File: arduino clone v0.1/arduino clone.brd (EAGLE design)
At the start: 72.9 x 27.6 mm, 47 parts, among them J203 ICSP HEADER, J402 FTDI Breakout Header, U101 ATMEGA328P_TQFP, U301 CH340G, Y101 16MHz, Y301 12MHz

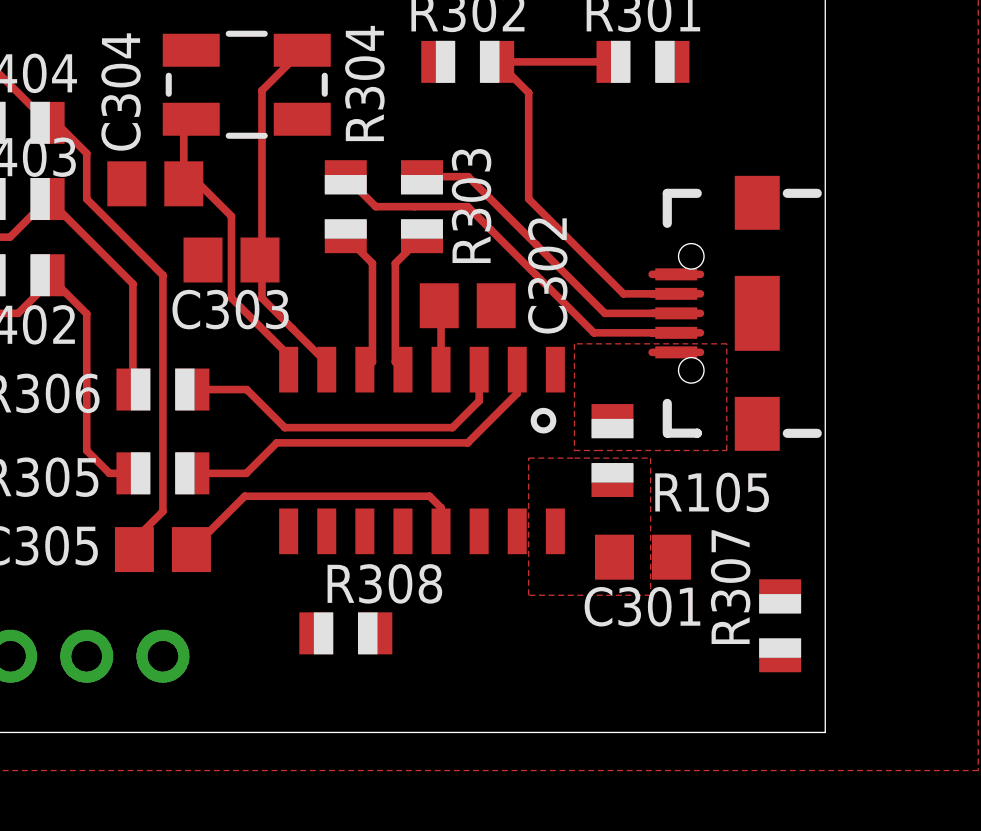
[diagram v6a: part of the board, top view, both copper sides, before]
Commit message: route and place R308 and R307
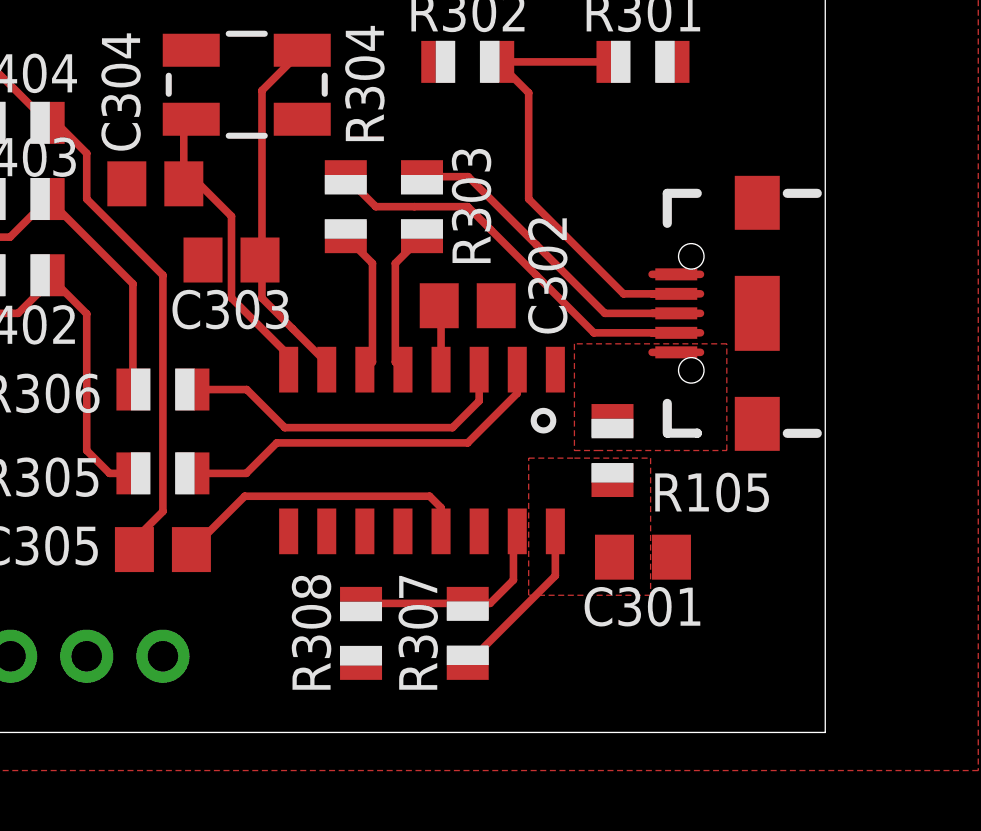
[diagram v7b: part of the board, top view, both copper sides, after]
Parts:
- moved R307 10.4 mm to (69.8, 41.4), turned to 270 degrees
- moved R308 0.51 mm to (66.3, 41.4), turned to 90 degrees
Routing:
- net CH340G_R232: track 0.00 -> 7.08 mm
- net PP5V0_CH340G: track 0.00 -> 5.61 mm
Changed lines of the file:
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@@
 <attribute name="NAME" x="53.594" y="48.768" size="1.27" layer="25"/>
 </element>
-<element name="R307" library="adafruit" package="R0805" value="10k" x="80.264" y="41.656" smashed="yes" rot="R90">
-<attribute name="NAME" x="79.248" y="40.894" size="1.27" layer="25" rot="R90"/>
-<attribute name="STUFF" value="NO STUFF" x="80.264" y="41.656" size="1.778" layer="27" rot="R90" display="off"/>
-</element>
-<element name="R308" library="adafruit" package="R0805" value="10k" x="65.786" y="41.402" smashed="yes">
-<attribute name="NAME" x="65.024" y="42.418" size="1.27" layer="25"/>
-<attribute name="STUFF" value="NO STUFF" x="65.786" y="41.402" size="1.778" layer="27" display="off"/>
+<element name="R307" library="adafruit" package="R0805" value="10k" x="69.85" y="41.402" smashed="yes" rot="R270">
+<attribute name="NAME" x="68.834" y="39.37" size="1.27" layer="25" rot="R90"/>
+<attribute name="STUFF" value="NO STUFF" x="69.85" y="41.402" size="1.778" layer="27" rot="R270" display="off"/>
+</element>
+<element name="R308" library="adafruit" package="R0805" value="10k" x="66.294" y="41.402" smashed="yes" rot="R90">
+<attribute name="NAME" x="65.278" y="39.37" size="1.27" layer="25" rot="R90"/>
+<attribute name="STUFF" value="NO STUFF" x="66.294" y="41.402" size="1.778" layer="27" rot="R90" display="off"/>
 </element>
 <element name="R401" library="adafruit" package="R0805" value="0" x="45.974" y="49.276" smashed="yes" rot="R270">
@@
 <vertex x="71.882" y="47.244"/>
 </polygon>
-<wire x1="74.742" y1="43.942" x2="80.264" y2="42.656" width="0" layer="19" extent="1-1"/>
+<wire x1="69.85" y1="40.402" x2="72.771" y2="43.323" width="0.254" layer="1"/>
+<wire x1="72.771" y1="43.323" x2="72.771" y2="44.803" width="0.254" layer="1"/>
 </signal>
 <signal name="PP3V3_CH340G">
@@
 <contactref element="R307" pad="1"/>
 <contactref element="R308" pad="2"/>
-<wire x1="71.501" y1="44.803" x2="80.264" y2="40.656" width="0" layer="19" extent="1-1"/>
-<wire x1="66.786" y1="41.402" x2="71.501" y2="44.803" width="0" layer="19" extent="1-1"/>
+<wire x1="66.294" y1="42.402" x2="69.85" y2="42.402" width="0.254" layer="1"/>
+<wire x1="71.501" y1="44.803" x2="71.374" y2="44.676" width="0.254" layer="1"/>
+<wire x1="71.374" y1="44.676" x2="71.374" y2="43.18" width="0.254" layer="1"/>
+<wire x1="71.374" y1="43.18" x2="70.596" y2="42.402" width="0.254" layer="1"/>
+<wire x1="70.596" y1="42.402" x2="69.85" y2="42.402" width="0.254" layer="1"/>
 </signal>
 <signal name="CH340G_XTAL_IN">
@@
 <wire x1="60.634" y1="58.54" x2="60.386" y2="58.292" width="0.254" layer="1"/>
 <wire x1="60.386" y1="58.292" x2="60.386" y2="56.388" width="0.254" layer="1"/>
-<wire x1="60.386" y1="56.388" x2="60.706" y2="56.388" width="0.254" layer="1"/>
 <wire x1="61.976" y1="55.306" x2="60.894" y2="56.388" width="0.254" layer="1"/>
 <wire x1="63.881" y1="50.193" x2="63.881" y2="50.673" width="0.254" layer="1"/>

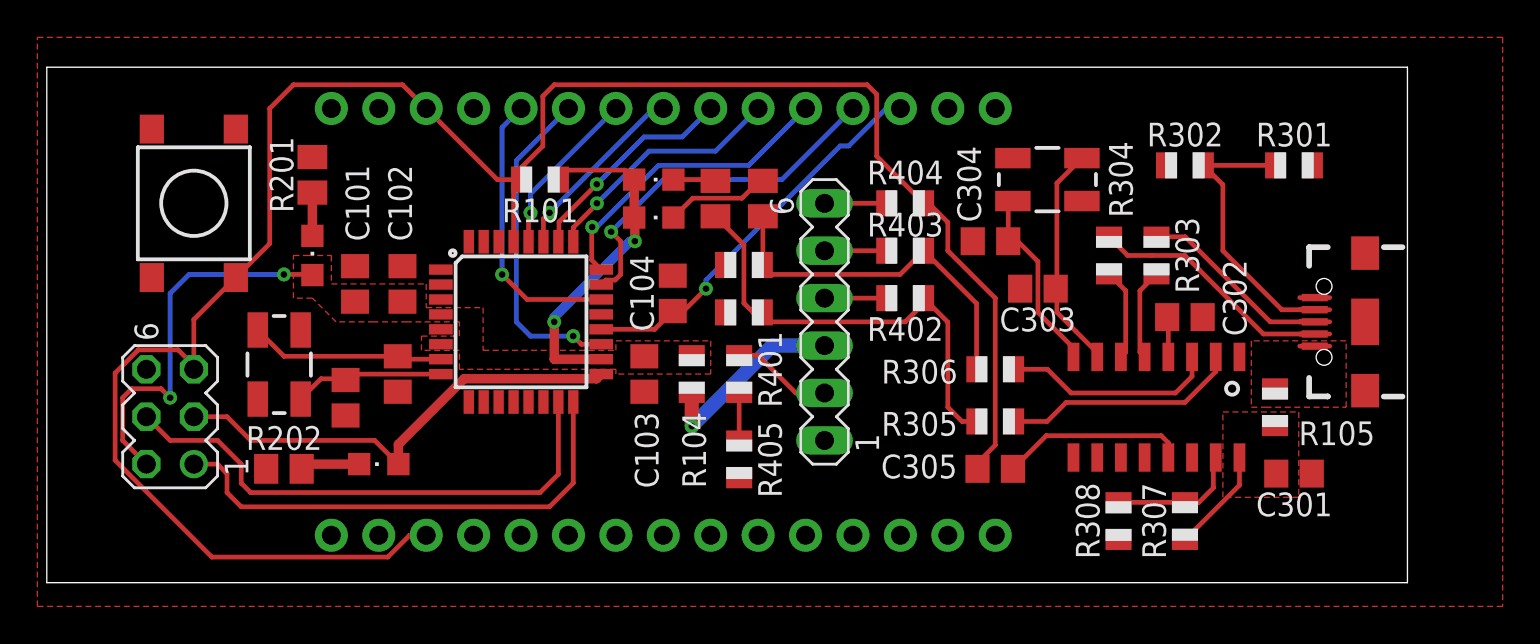
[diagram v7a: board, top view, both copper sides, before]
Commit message: add PP5V0_USB trace from USB port to FTDI header
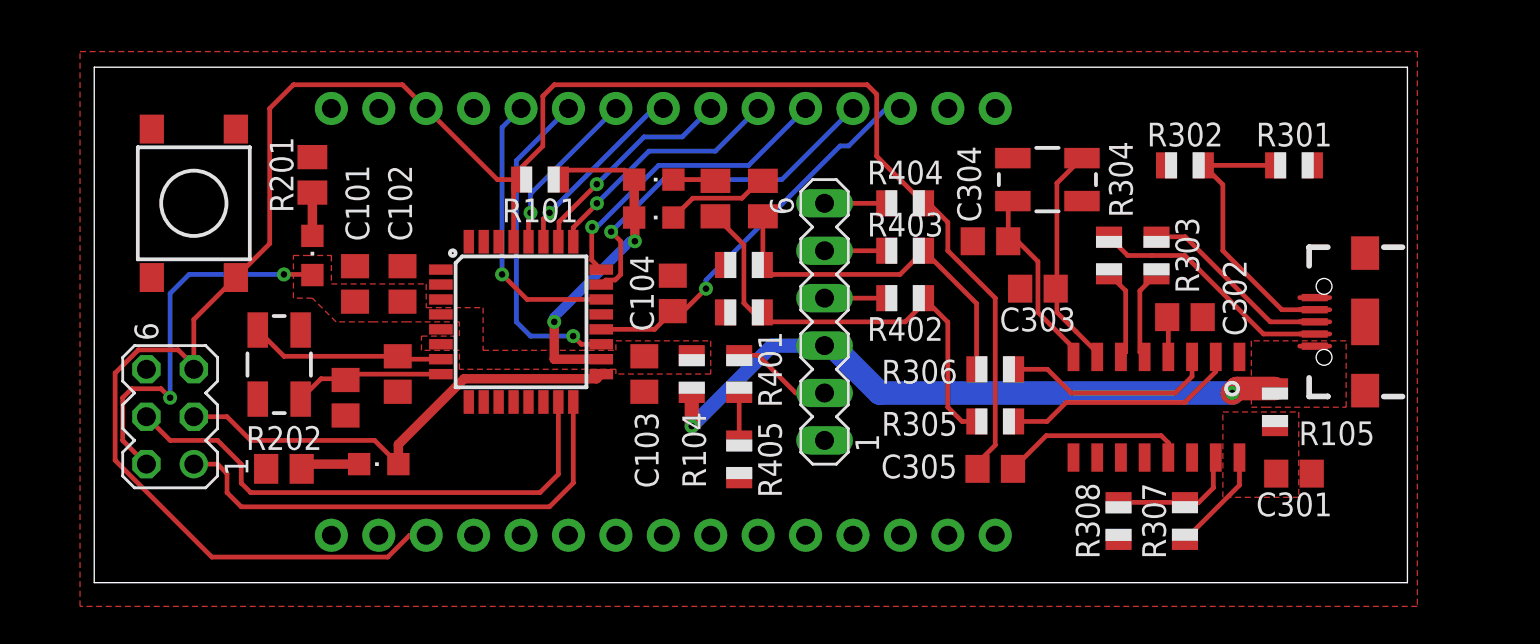
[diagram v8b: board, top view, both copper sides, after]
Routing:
- net PP5V0_USB: track 10.7 -> 36.0 mm, vias 1 -> 2
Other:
- board size 72.9 x 27.6 mm -> 70.3 x 27.6 mm
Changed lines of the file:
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@@
 <board>
 <plain>
-<wire x1="8.89" y1="38.1" x2="81.768" y2="38.1" width="0" layer="20"/>
+<wire x1="11.43" y1="38.1" x2="81.768" y2="38.1" width="0" layer="20"/>
 <wire x1="81.768" y1="38.1" x2="81.768" y2="65.71" width="0" layer="20"/>
-<wire x1="81.768" y1="65.71" x2="8.89" y2="65.71" width="0" layer="20"/>
-<wire x1="8.89" y1="65.71" x2="8.89" y2="38.1" width="0" layer="20"/>
+<wire x1="81.768" y1="65.71" x2="11.43" y2="65.71" width="0" layer="20"/>
+<wire x1="11.43" y1="65.71" x2="11.43" y2="38.1" width="0" layer="20"/>
 </plain>
 <attributes>
@@
 <contactref element="R202" pad="1"/>
 <polygon width="0.0762" layer="1" rank="6">
-<vertex x="8.382" y="67.31"/>
-<vertex x="86.868" y="67.31"/>
-<vertex x="86.868" y="36.83"/>
-<vertex x="8.382" y="36.83"/>
+<vertex x="10.668" y="66.548"/>
+<vertex x="82.296" y="66.548"/>
+<vertex x="82.296" y="36.83"/>
+<vertex x="10.668" y="36.83"/>
 </polygon>
 </signal>
@@
 <wire x1="43.434" y1="46.482" x2="47.752" y2="50.8" width="0.762" layer="16"/>
 <wire x1="47.752" y1="50.8" x2="50.546" y2="50.8" width="0.762" layer="16"/>
+<wire x1="74.676" y1="48.498" x2="72.628" y2="48.498" width="1.27" layer="1"/>
+<wire x1="72.628" y1="48.498" x2="72.39" y2="48.26" width="1.27" layer="1"/>
+<via x="72.39" y="48.26" extent="1-16" drill="0.35"/>
+<wire x1="72.39" y1="48.26" x2="53.4991875" y2="48.26" width="1.27" layer="16"/>
+<wire x1="53.4991875" y1="48.26" x2="50.9591875" y2="50.8" width="1.27" layer="16"/>
 <wire x1="76.802" y1="50.77" x2="76.692" y2="60.452" width="0" layer="19" extent="1-1"/>
-<wire x1="57.15" y1="63.5" x2="76.692" y2="60.452" width="0" layer="19" extent="1-1"/>
-<wire x1="50.546" y1="50.8" x2="57.15" y2="63.5" width="0" layer="19" extent="1-1"/>
+<wire x1="57.15" y1="63.5" x2="50.9591875" y2="50.8" width="0" layer="19" extent="1-1"/>
 <wire x1="31.75" y1="63.5" x2="43.434" y2="48.276" width="0" layer="19" extent="1-1"/>
 <wire x1="24.13" y1="63.5" x2="31.75" y2="63.5" width="0" layer="19" extent="1-1"/>
+<wire x1="50.9591875" y1="50.8" x2="50.546" y2="50.8" width="1.27" layer="16"/>
 </signal>
 <signal name="PP5V0_CH340G">
